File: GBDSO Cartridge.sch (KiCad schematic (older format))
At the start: 75 parts, among them J1 MJ-3523-SMT-TR, J2 MJ-3523-SMT-TR, J3 EdgeConnector, J5 Conn_01x02, J6 Conn_01x02, P1 100k, P2 100k, SW1 SW_SPDT, SW2 SW_SPDT, U1 TL062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

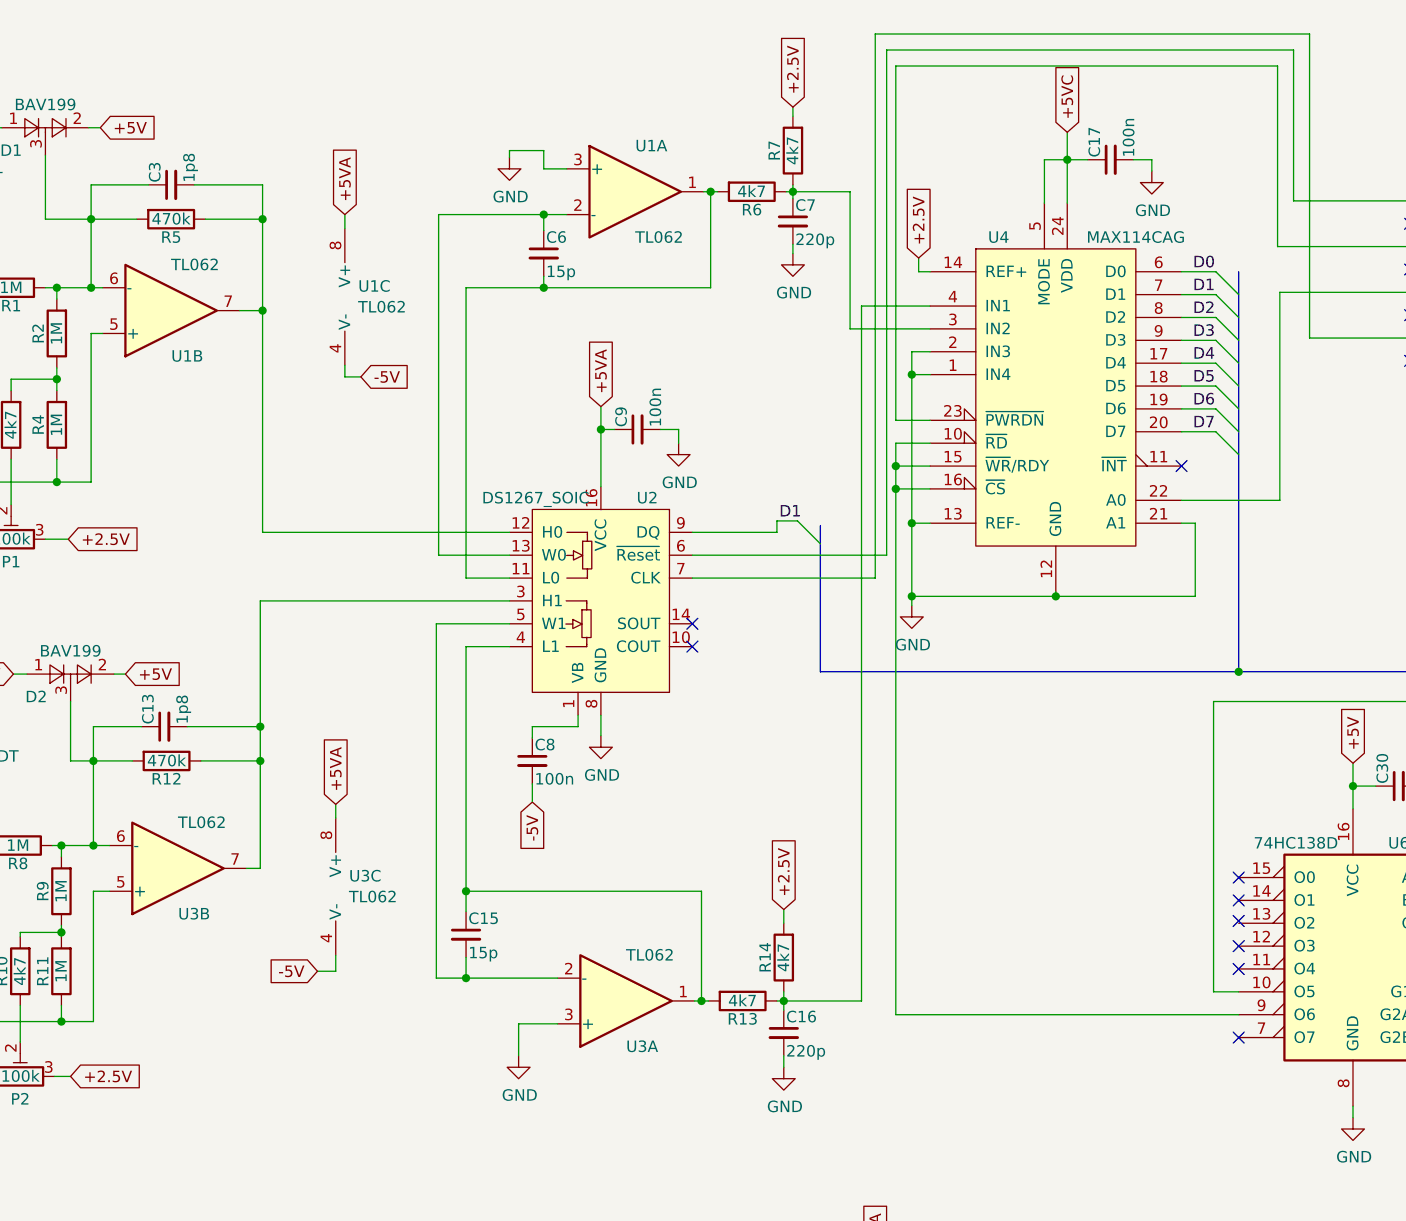
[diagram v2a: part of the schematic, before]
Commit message: changed TL062 to TL072, see #14. updated schematic image, see #9.
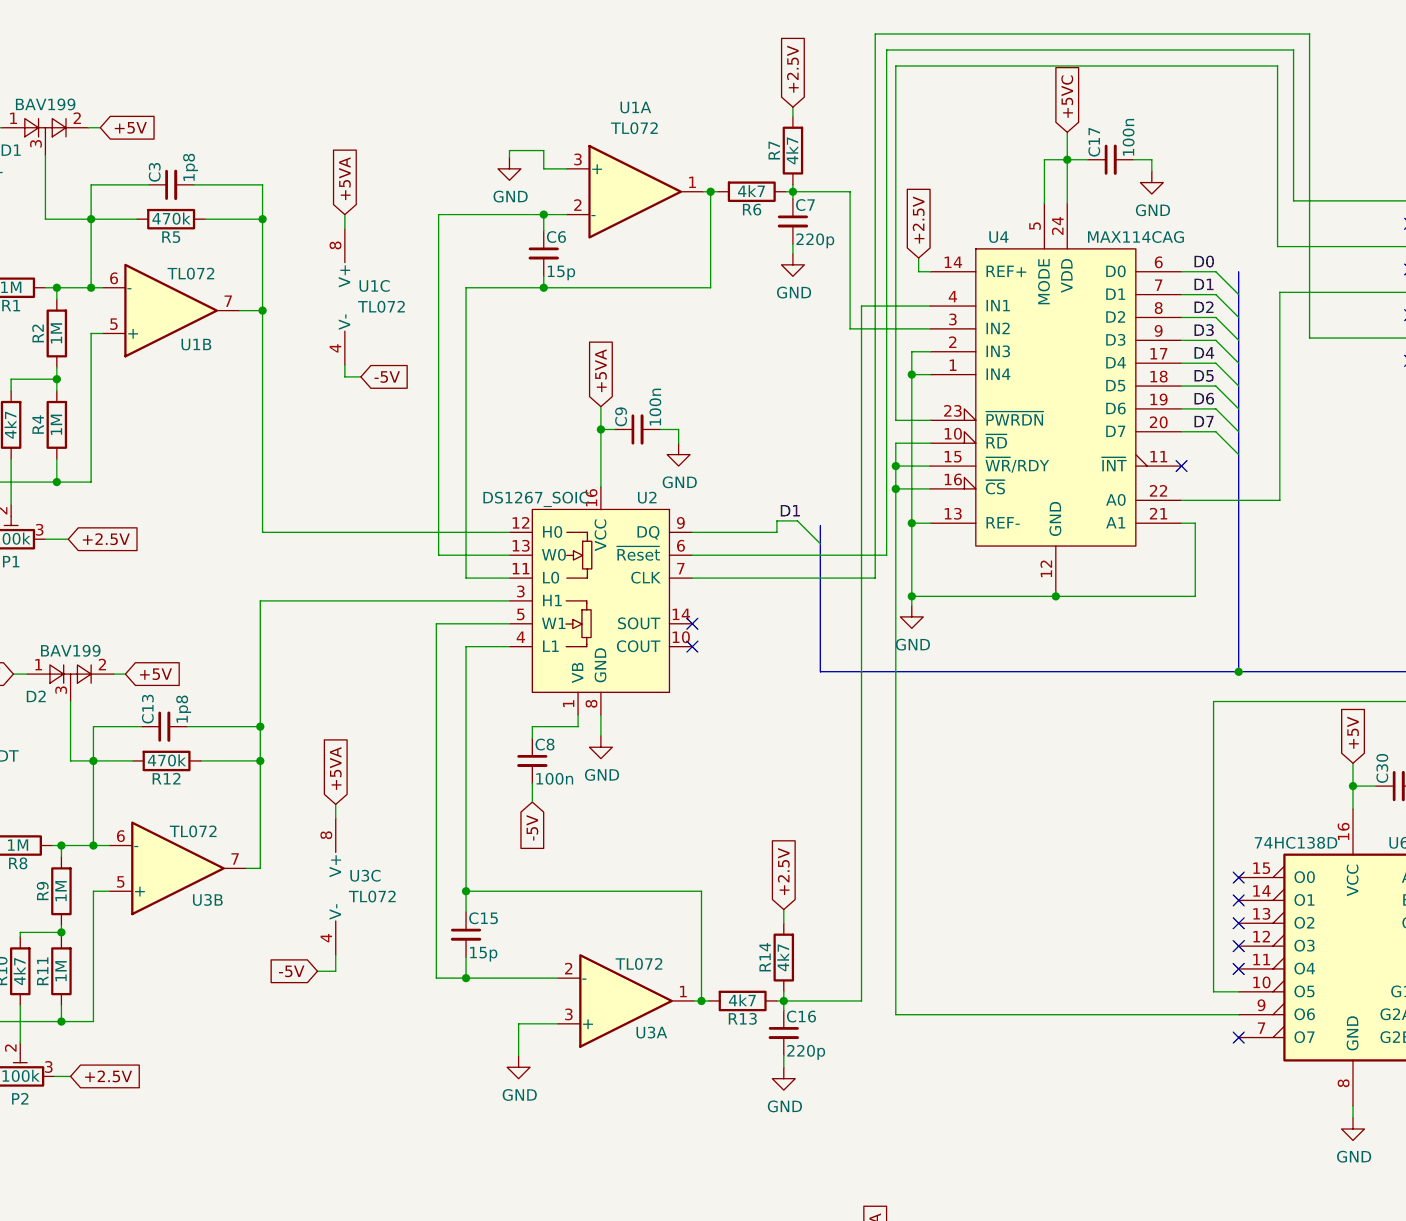
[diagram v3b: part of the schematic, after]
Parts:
- removed U1, U3: TL062, Package_SO:SOIC-8_3.9x4.9mm_P1.27mm, symbol Amplifier_Operational:TL062
- added U1, U3: TL072, Package_SO:SOIC-8_3.9x4.9mm_P1.27mm, symbol Amplifier_Operational:TL072
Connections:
- net +5VA: now also U1.8 (V+), U3.8 (V+)
- net -5V: now also U1.4 (V-), U3.4 (V-)
- net GND: now also U1.3 (+), U1.5 (+), U3.3 (+), U3.5 (+)
- net at C6.2, R6.2, U2.11 (L0): now also U1.1
- net at C6.1, U2.13 (W0): now also U1.2 (-)
- net at C3.1, D1.3, R1.1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: now also U1.6 (-)
- net at C3.2, R5.1, U2.12 (H0): now also U1.7
- net at C15.1, R13.2, U2.4 (L1): now also U3.1
- net at C15.2, U2.5 (W1): now also U3.2 (-)
- net at C13.1, D2.3, R12.2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: now also U3.6 (-)
- net at C13.2, R12.1, U2.3 (H1): now also U3.7
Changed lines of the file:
@@
 EESchema Schematic File Version 4
-LIBS:GBDSO-cache
-EELAYER 29 0
+EELAYER 30 0
 EELAYER END
 $Descr A4 11693 8268
@@
 Comment4 ""
 $EndDescr
-$Comp
-L Amplifier_Operational:TL062 U1
-U 1 1 5C828B36
-P 4610 1200
-F 0 "U1" H 4610 1400 50  0000 L CNN
-F 1 "TL062" H 4610 1000 50  0000 L CNN
-F 2 "Package_SO:SOIC-8_3.9x4.9mm_P1.27mm" H 4610 1200 50  0001 C CNN
-F 3 "" H 4610 1200 50  0001 C CNN
-	1    4610 1200
-	1    0    0    -1
-$EndComp
-$Comp
-L Amplifier_Operational:TL062 U1
-U 2 1 5C828B3D
-P 2580 1720
-F 0 "U1" H 2580 1920 50  0000 L CNN
-F 1 "TL062" H 2580 1520 50  0000 L CNN
-F 2 "Package_SO:SOIC-8_3.9x4.9mm_P1.27mm" H 2580 1720 50  0001 C CNN
-F 3 "" H 2580 1720 50  0001 C CNN
-	2    2580 1720
-	1    0    0    1
-$EndComp
-$Comp
-L Amplifier_Operational:TL062 U3
-U 1 1 5C828B44
-P 4570 4740
-F 0 "U3" H 4570 4940 50  0000 L CNN
-F 1 "TL062" H 4570 4540 50  0000 L CNN
-F 2 "Package_SO:SOIC-8_3.9x4.9mm_P1.27mm" H 4570 4740 50  0001 C CNN
-F 3 "" H 4570 4740 50  0001 C CNN
-	1    4570 4740
-	1    0    0    1
-$EndComp
-$Comp
-L Amplifier_Operational:TL062 U3
-U 2 1 5C828B4B
-P 2610 4160
-F 0 "U3" H 2610 4360 50  0000 L CNN
-F 1 "TL062" H 2610 3960 50  0000 L CNN
-F 2 "Package_SO:SOIC-8_3.9x4.9mm_P1.27mm" H 2610 4160 50  0001 C CNN
-F 3 "" H 2610 4160 50  0001 C CNN
-	2    2610 4160
-	1    0    0    1
-$EndComp
 $Comp
 L Potentiometer_Digital:DS1267_SOIC U2
@@
 NoConn ~ 7250 4600
 NoConn ~ 7250 4500
-NoConn ~ 7250 4390
+NoConn ~ 7250 4400
 NoConn ~ 7250 4300
 NoConn ~ 7250 4200
@@
 NoConn ~ 10640 6090
 $Comp
-L Amplifier_Operational:TL062 U1
-U 3 1 5C829067
-P 3440 1660
-F 0 "U1" H 3398 1706 50  0000 L CNN
-F 1 "TL062" H 3398 1615 50  0000 L CNN
-F 2 "" H 3440 1660 50  0001 C CNN
-F 3 "http://www.ti.com/lit/ds/symlink/tl061.pdf" H 3440 1660 50  0001 C CNN
-	3    3440 1660
-	1    0    0    -1
-$EndComp
-$Comp
-L Amplifier_Operational:TL062 U3
-U 3 1 5C82906E
-P 3400 4240
-F 0 "U3" H 3358 4286 50  0000 L CNN
-F 1 "TL062" H 3358 4195 50  0000 L CNN
-F 2 "" H 3400 4240 50  0001 C CNN
-F 3 "http://www.ti.com/lit/ds/symlink/tl061.pdf" H 3400 4240 50  0001 C CNN
-	3    3400 4240
-	1    0    0    -1
-$EndComp
-$Comp
 L Jumper:SolderJumper_3_Open JP1
 U 1 1 5C829077
@@
 Text Notes 1020 4420 0    50   ~ 0
 CH A
+$Comp
+L Amplifier_Operational:TL072 U1
+U 1 1 5E8728C5
+P 4610 1200
+F 0 "U1" H 4610 1567 50  0000 C CNN
+F 1 "TL072" H 4610 1476 50  0000 C CNN
+F 2 "Package_SO:SOIC-8_3.9x4.9mm_P1.27mm" H 4610 1200 50  0001 C CNN
+F 3 "http://www.ti.com/lit/ds/symlink/tl071.pdf" H 4610 1200 50  0001 C CNN
+	1    4610 1200
+	1    0    0    -1
+$EndComp
+$Comp
+L Amplifier_Operational:TL072 U1
+U 2 1 5E87600C
+P 2580 1720
+F 0 "U1" H 2690 1870 50  0000 C CNN
+F 1 "TL072" H 2670 1560 50  0000 C CNN
+F 2 "Package_SO:SOIC-8_3.9x4.9mm_P1.27mm" H 2580 1720 50  0001 C CNN
+F 3 "http://www.ti.com/lit/ds/symlink/tl071.pdf" H 2580 1720 50  0001 C CNN
+	2    2580 1720
+	1    0    0    1
+$EndComp
+$Comp
+L Amplifier_Operational:TL072 U1
+U 3 1 5E879A8F
+P 3440 1660
+F 0 "U1" H 3398 1706 50  0000 L CNN
+F 1 "TL072" H 3398 1615 50  0000 L CNN
+F 2 "Package_SO:SOIC-8_3.9x4.9mm_P1.27mm" H 3440 1660 50  0001 C CNN
+F 3 "http://www.ti.com/lit/ds/symlink/tl071.pdf" H 3440 1660 50  0001 C CNN
+	3    3440 1660
+	1    0    0    -1
+$EndComp
+$Comp
+L Amplifier_Operational:TL072 U3
+U 1 1 5E87C68F
+P 4570 4740
+F 0 "U3" H 4680 4880 50  0000 C CNN
+F 1 "TL072" H 4630 4580 50  0000 C CNN
+F 2 "Package_SO:SOIC-8_3.9x4.9mm_P1.27mm" H 4570 4740 50  0001 C CNN
+F 3 "http://www.ti.com/lit/ds/symlink/tl071.pdf" H 4570 4740 50  0001 C CNN
+	1    4570 4740
+	1    0    0    1
+$EndComp
+$Comp
+L Amplifier_Operational:TL072 U3
+U 2 1 5E8809F8
+P 2610 4160
+F 0 "U3" H 2740 4300 50  0000 C CNN
+F 1 "TL072" H 2680 4000 50  0000 C CNN
+F 2 "Package_SO:SOIC-8_3.9x4.9mm_P1.27mm" H 2610 4160 50  0001 C CNN
+F 3 "http://www.ti.com/lit/ds/symlink/tl071.pdf" H 2610 4160 50  0001 C CNN
+	2    2610 4160
+	1    0    0    1
+$EndComp
+$Comp
+L Amplifier_Operational:TL072 U3
+U 3 1 5E882FE2
+P 3400 4240
+F 0 "U3" H 3358 4286 50  0000 L CNN
+F 1 "TL072" H 3358 4195 50  0000 L CNN
+F 2 "Package_SO:SOIC-8_3.9x4.9mm_P1.27mm" H 3400 4240 50  0001 C CNN
+F 3 "http://www.ti.com/lit/ds/symlink/tl071.pdf" H 3400 4240 50  0001 C CNN
+	3    3400 4240
+	1    0    0    -1
+$EndComp
 Wire Bus Line
 	5420 2660 5420 3300

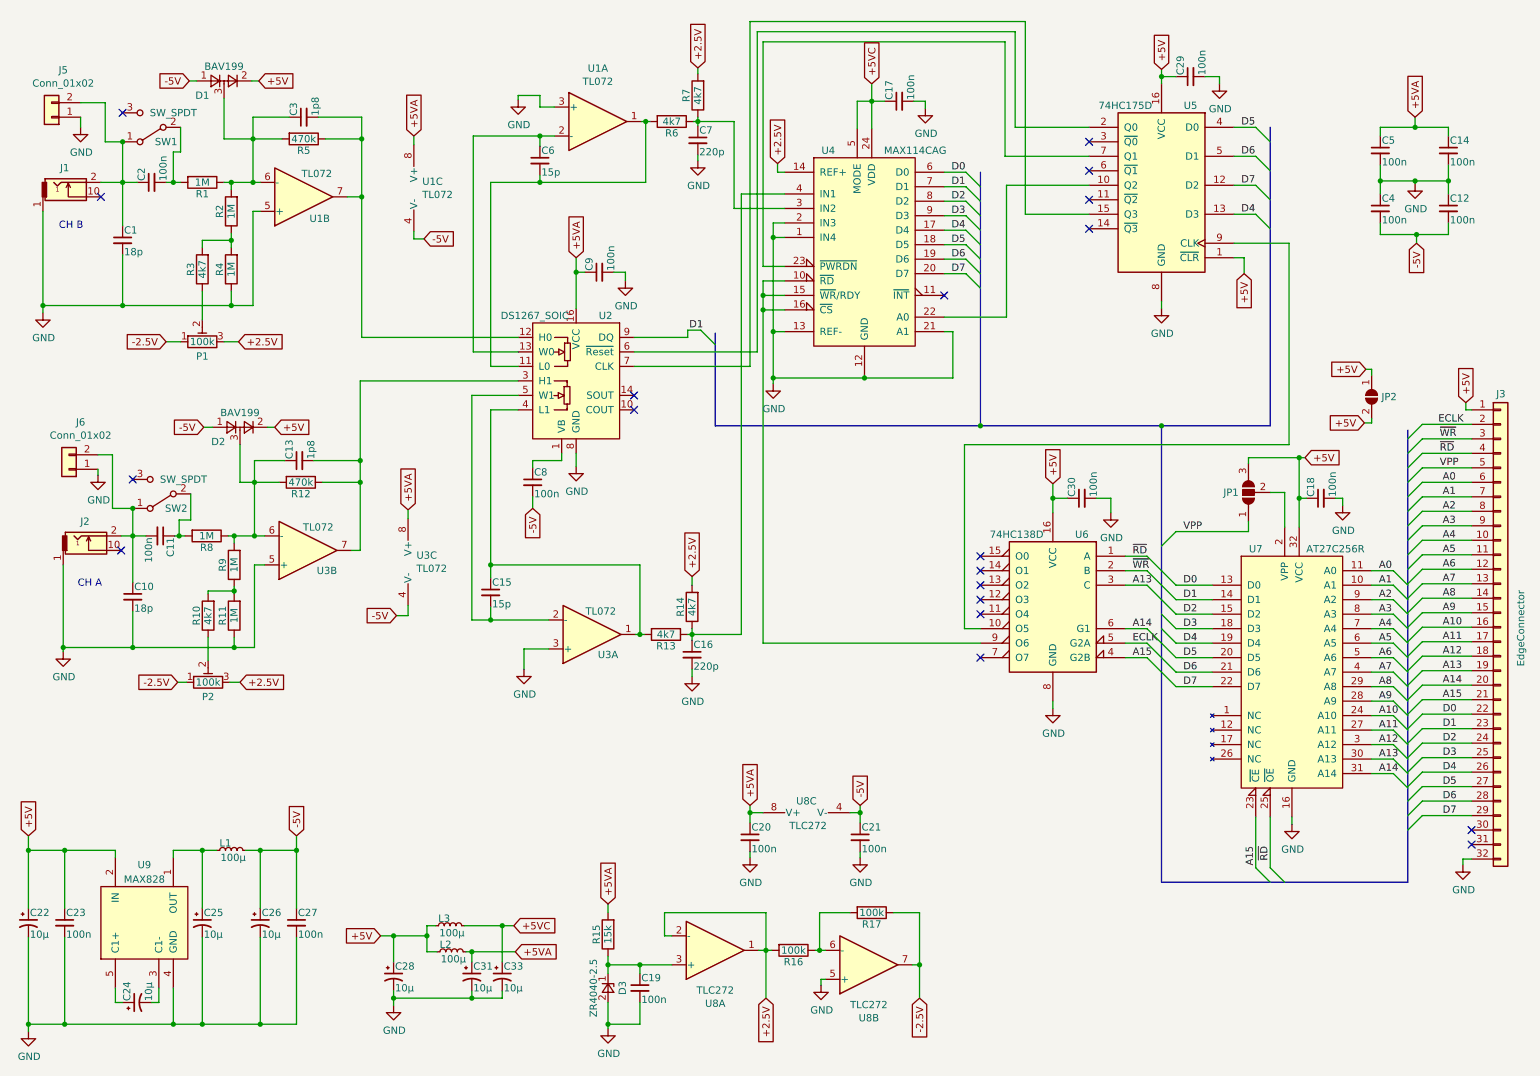
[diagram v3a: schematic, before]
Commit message: moved C4, C5, C12, C14 to the power pins of the TL072
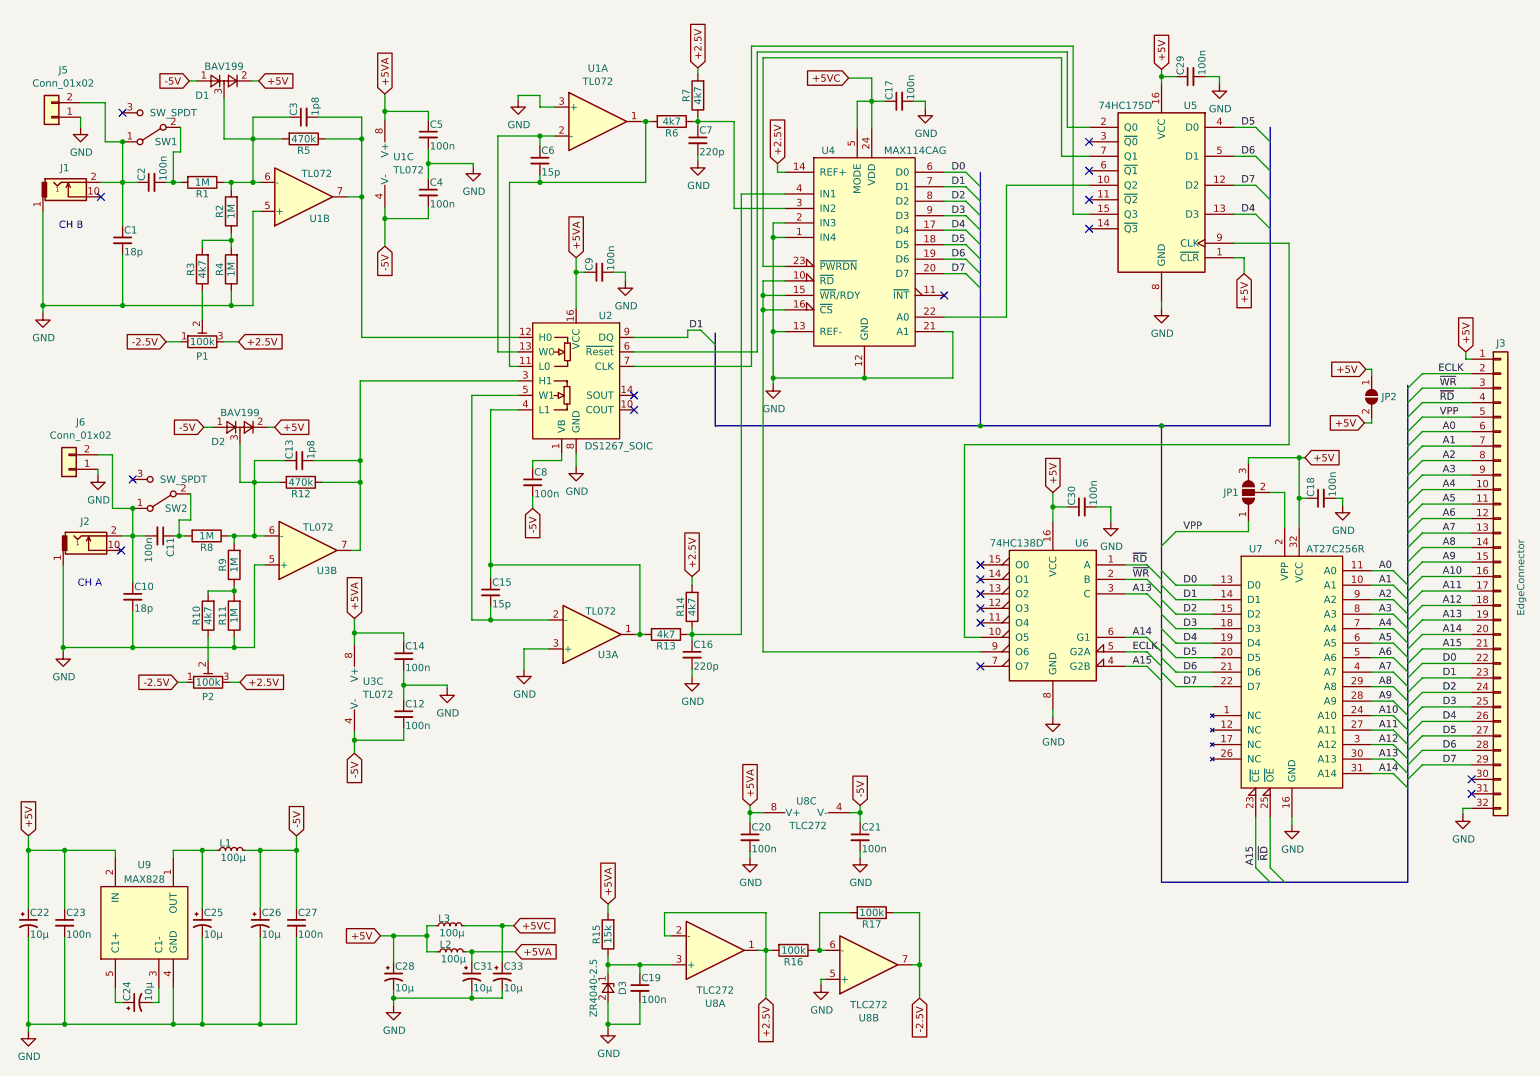
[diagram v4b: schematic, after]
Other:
- moved on the sheet: C12, C14, C30, C4, C5, J3, U1C, U3C, U6

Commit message: fix #16
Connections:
- net A14: now also U6.4 (G2B); no longer U6.6 (G1)
- net A15: now also U6.6 (G1); no longer U6.4 (G2B)
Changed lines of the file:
@@
 Text Label 8300 4460 0    50   ~ 0
 A13
-Text Label 8300 4760 0    50   ~ 0
+Text Label 8310 4960 0    50   ~ 0
 A14
 Text Label 8300 4860 0    50   ~ 0
 ECLK
-Text Label 8300 4960 0    50   ~ 0
+Text Label 8300 4760 0    50   ~ 0
 A15
 Entry Wire Line

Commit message: fix #17
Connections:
- net +5V: no longer D1.2, D2.2
- net +5VA: now also D1.2
- new net +5Va: D2.2
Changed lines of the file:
@@
 	1790 920  1840 920
 Text GLabel 2270 920  2    50   Input ~ 0
-+5V
++5VA
 Wire Wire Line
 	2270 920  2220 920
@@
 	1890 3310 1950 3310
 Text GLabel 2380 3310 2    50   Input ~ 0
-+5V
++5Va
 Wire Wire Line
 	2380 3310 2330 3310
